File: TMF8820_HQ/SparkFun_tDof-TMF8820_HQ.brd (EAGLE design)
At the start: 25.4 x 12.7 mm, 48 parts, among them J4 QWIIC_RIGHT_ANGLE, J5 QWIIC_RIGHT_ANGLE

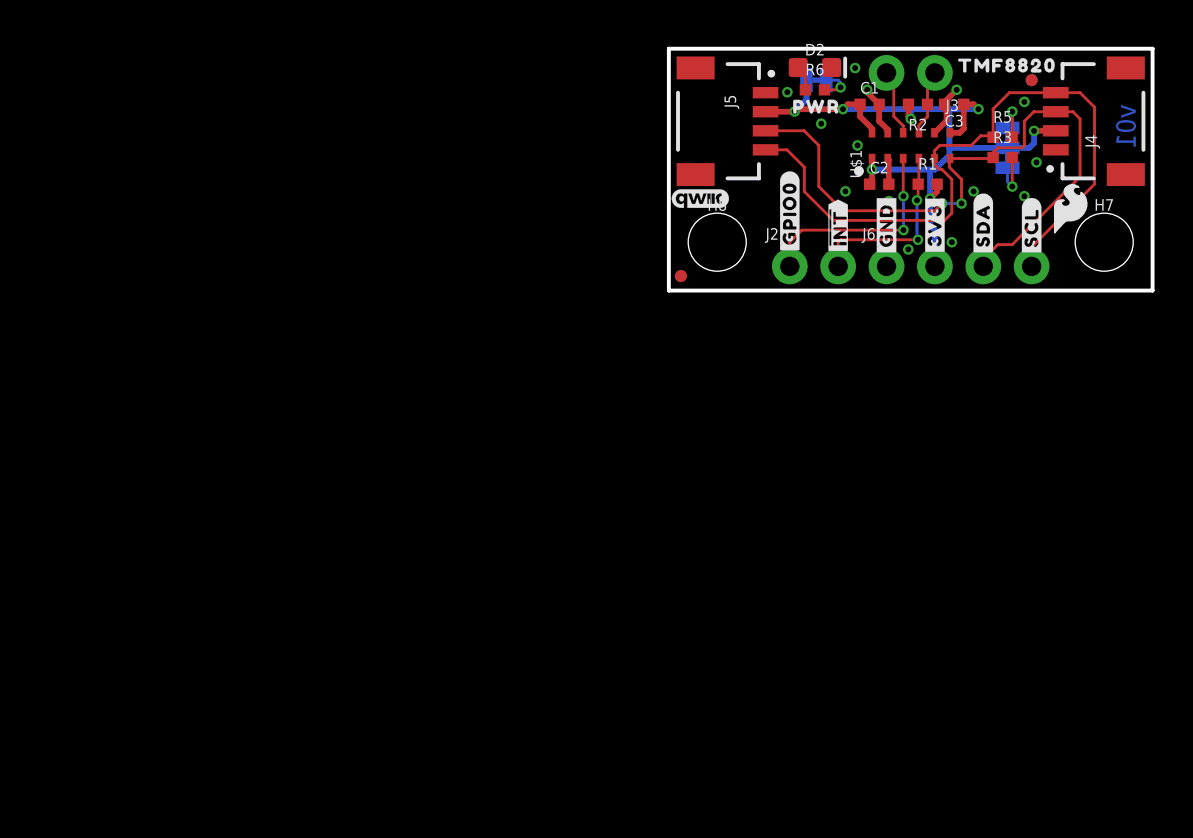
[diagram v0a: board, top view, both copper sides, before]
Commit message: Adds default address to HQ boards, fixes some clearance issues
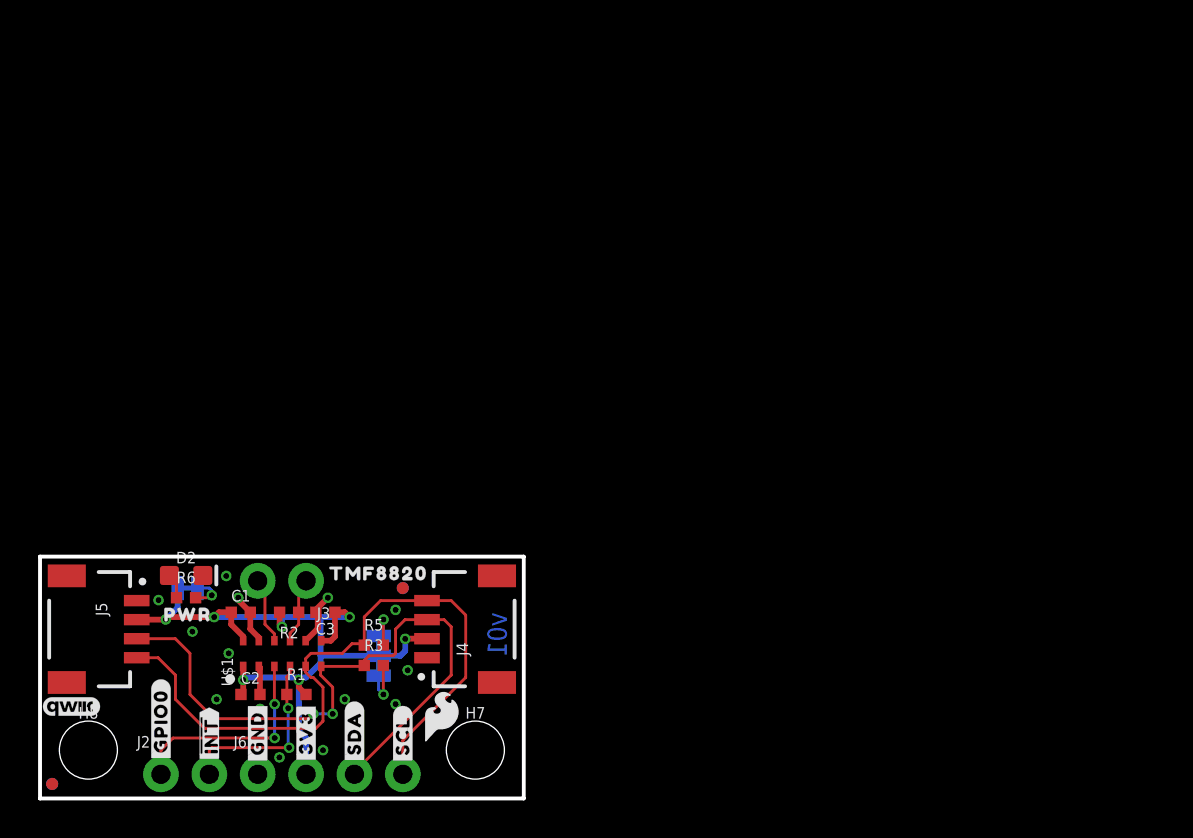
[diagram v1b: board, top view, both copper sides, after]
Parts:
- moved R1 42.6 mm to (13.5, 5.46)
- moved C2 42.5 mm to (11.0, 5.46)
- moved D2 42.4 mm to (7.67, 11.7)
- moved FD5 42.4 mm to (19.1, 11.0)
- moved FD6 42.4 mm to (0.64, 0.76)
- moved FD7 42.4 mm to (0.64, 0.76)
- moved FD8 42.4 mm to (19.1, 11.0)
- moved H7 42.4 mm to (22.9, 2.54)
- moved H8 42.4 mm to (2.54, 2.54)
- moved J2 42.4 mm to (6.35, 1.27)
- moved J3 42.4 mm to (14.0, 11.4)
- moved J4 42.4 mm to (20.3, 8.89)
- moved J5 42.4 mm to (5.08, 8.89)
- moved J6 42.4 mm to (11.4, 1.27)
- moved LED 42.4 mm to (7.75, 11.0)
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
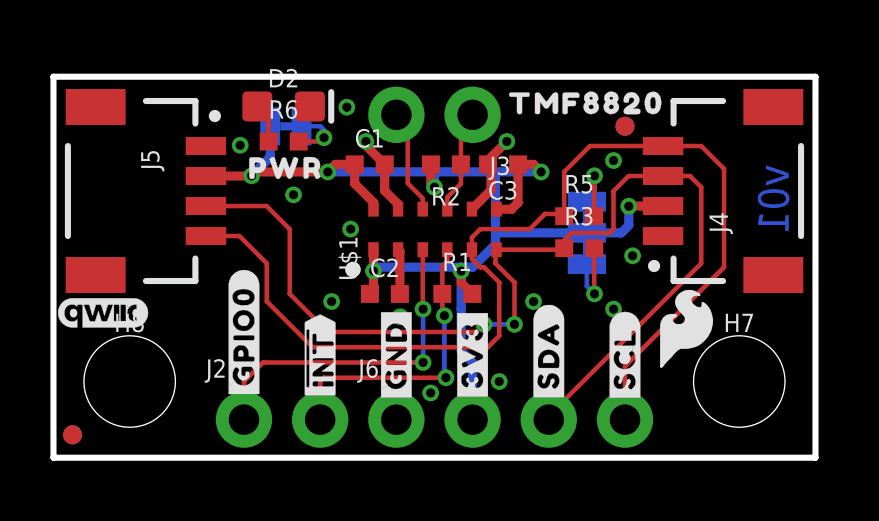
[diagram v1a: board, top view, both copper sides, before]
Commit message: Updates the TMF882X device in the library to have two variants of the two ICs
* Better silk labeling for the 8820 and 8820 HQ
* Adds new IC variants to both designs
* Adds default addresses to schematics
* Moves some traces and vias for better ground pour in the 8820 design
* Moves entire 8820 design to origin in board file
* Adds measure from center of qwiic connector to edge in 8820 design
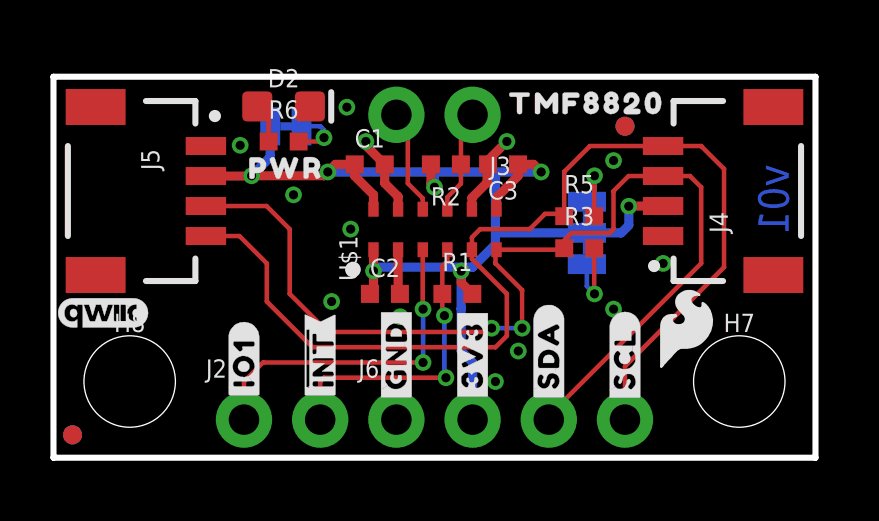
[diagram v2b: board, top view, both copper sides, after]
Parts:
- removed U$17: (no value), TMFHQBotSilk:#GPIO1#8
- removed U$21: (no value), TMFHQTopSilk:##INT##20
- removed U$24: (no value), TMFHQTopSilk:TMF882021
- removed U$32: (no value), TMFHQTopSilk:DTOF8821882023
- removed U$42: (no value), TMFHQTopSilk:#GPIO0#19
- added U$2: (no value), TMFHQBotSilk:#IO1#8
- added U$4: (no value), TMFHQTopSilk:##INT##8
- added U$6: (no value), TMFHQTopSilk:#IO1#8
- added U$7: (no value), TMFHQTopSilk:DTOF882188211
- added U$8: (no value), TMFHQTopSilk:TMF88209
- U$1: value TMF8820- -> TMF882X_TMF8820
- renumbered U$23 to U$5, U$41 to U$3
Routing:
- net GND: track 6.63 -> 6.61 mm, vias 14 -> 13
